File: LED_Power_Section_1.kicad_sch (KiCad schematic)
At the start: 9 parts, among them IC3 A6214KLKTR-T

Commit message: reviewed
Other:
- moved on the sheet: C1, C6, C7, C8, D2, IC3, L2, R4, R5

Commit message: first complete version schematics
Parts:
- added C11, C24, C28, C32, C36: 33 uF, Capacitor_THT:CP_Radial_D8.0mm_P3.50mm, symbol PCM_SL_Devices:Capacitor_PO
- added C21, C25, C29, C33, C37: 4.7 uF, Capacitor_THT:C_Disc_D3.0mm_W2.0mm_P2.50mm, symbol PCM_SL_Devices:Capacitor_NP
- added C22, C26, C30, C34, C38: 1 uF, Capacitor_SMD:C_1206_3216Metric_Pad1.33x1.80mm_HandSolder, symbol PCM_SL_Devices:Capacitor_NP
- added C23, C27, C31, C35, C39: 0.1 uF, Capacitor_SMD:C_1206_3216Metric_Pad1.33x1.80mm_HandSolder, symbol PCM_SL_Devices:Capacitor_NP
- added D3, D4, D5, D6, D7: 30V 2A, ADC:SODFL3516X90N, symbol PCM_4ms_Diode:B140-E3
- added IC4, IC5, IC6, IC7, IC8: A6214KLKTR-T, LED_Driver:SOP100P600X165-11N, symbol A6214KLKTR-T:A6214KLKTR-T
- added L3, L4, L5, L6, L7: 47 uH 2A, ADC:CDRH105RNP151NC, symbol Device:L
- added R11, R13, R15, R17, R19: 442k, Resistor_SMD:R_1206_3216Metric_Pad1.30x1.75mm_HandSolder, symbol PCM_SL_Resistors:Resistor
- added R12, R14, R16, R18, R20: R120 or R260, Resistor_THT:R_Radial_Power_L16.1mm_W9.0mm_P7.37mm, symbol PCM_SL_Resistors:Resistor
- D2: value 60V 2A -> 30V 2A
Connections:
- net +12V: now also C11.1, C21.2, C24.1, C25.2, C28.1, C29.2, C32.1, C33.2, C36.1, C37.2, IC4.1 (VIN), IC5.1 (VIN), IC6.1 (VIN), IC7.1 (VIN), IC8.1 (VIN), R11.2, R13.2, R15.2, R17.2, R19.2
- net GND: now also C11.2, C21.1, C22.1, C24.2, C25.1, C26.1, C28.2, C29.1, C30.1, C32.2, C33.1, C34.1, C36.2, C37.1, C38.1, D3.2 (A), D4.2 (A), D5.2 (A), D6.2 (A), D7.2 (A), IC4.11 (GND_2), IC4.6 (GND_1), IC5.11 (GND_2), IC5.6 (GND_1), IC6.11 (GND_2), IC6.6 (GND_1), IC7.11 (GND_2), IC7.6 (GND_1), IC8.11 (GND_2), IC8.6 (GND_1)
- new net: C31.2, D5.1 (K), IC6.10 (SW), L5.1
- new net: C27.2, D4.1 (K), IC5.10 (SW), L4.1
- new net: C39.2, D7.1 (K), IC8.10 (SW), L7.1
- new net: IC8.2 (TON), R19.1
- new net: C38.2, IC8.4 (ADIM), IC8.5 (VCC)
- new net: C39.1, IC8.9 (BOOT)
- new net: C30.2, IC6.4 (ADIM), IC6.5 (VCC)
- new net: C26.2, IC5.4 (ADIM), IC5.5 (VCC)
- new net: IC6.2 (TON), R15.1
- new net: C31.1, IC6.9 (BOOT)
- new net: IC4.2 (TON), R11.1
- new net: C34.2, IC7.4 (ADIM), IC7.5 (VCC)
- new net: IC5.2 (TON), R13.1
- new net: C27.1, IC5.9 (BOOT)
- new net: C35.2, D6.1 (K), IC7.10 (SW), L6.1
- new net: C23.2, D3.1 (K), IC4.10 (SW), L3.1
- new net: C35.1, IC7.9 (BOOT)
- new net: C22.2, IC4.4 (ADIM), IC4.5 (VCC)
- new net: C23.1, IC4.9 (BOOT)
- new net: IC7.2 (TON), R17.1
- new net I_LED_1: IC4.8 (CSH), L3.2, R12.2
- new net I_LED_2: IC5.8 (CSH), L4.2, R14.2
- new net I_LED_3: IC6.8 (CSH), L5.2, R16.2
- new net I_LED_4: IC7.8 (CSH), L6.2, R18.2
- new net I_LED_5: IC8.8 (CSH), L7.2, R20.2
- new net LED_1: IC4.7 (CSL), R12.1
- new net LED_2: IC5.7 (CSL), R14.1
- new net LED_3: IC6.7 (CSL), R16.1
- new net LED_4: IC7.7 (CSL), R18.1
- new net LED_5: IC8.7 (CSL), R20.1
- new net PWM_1: IC4.3 (EN/PWM)
- new net PWM_2: IC5.3 (EN/PWM)
- new net PWM_3: IC6.3 (EN/PWM)
- new net PWM_4: IC7.3 (EN/PWM)
- new net PWM_5: IC8.3 (EN/PWM)
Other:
- moved on the sheet: C1, C6, C7, C8, D2, IC3, L2, R4, R5

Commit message: Changed footprints of passive elements, reviewed
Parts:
- removed C1, C11, C24, C28, C32, C36: 33 uF, Capacitor_THT:CP_Radial_D8.0mm_P3.50mm, symbol PCM_SL_Devices:Capacitor_PO
- removed C21, C25, C29, C33, C37, C6: 4.7 uF, Capacitor_THT:C_Disc_D3.0mm_W2.0mm_P2.50mm, symbol PCM_SL_Devices:Capacitor_NP
- removed C22, C26, C30, C34, C38, C7: 1 uF, Capacitor_SMD:C_1206_3216Metric_Pad1.33x1.80mm_HandSolder, symbol PCM_SL_Devices:Capacitor_NP
- removed C23, C27, C31, C35, C39, C8: 0.1 uF, Capacitor_SMD:C_1206_3216Metric_Pad1.33x1.80mm_HandSolder, symbol PCM_SL_Devices:Capacitor_NP
- added C14, C15, C16, C29, C30, C31: 22uF, Capacitor_SMD:C_0805_2012Metric_Pad1.18x1.45mm_HandSolder, symbol Device:C_Small
- added C17, C18, C19, C32, C33, C34: 4,7uF, Capacitor_SMD:C_0603_1608Metric_Pad1.08x0.95mm_HandSolder, symbol Device:C_Small
- added C20, C21, C22, C35, C36, C37: 1uF, Capacitor_SMD:C_0603_1608Metric_Pad1.08x0.95mm_HandSolder, symbol Device:C_Small
- added C23, C24, C25, C26, C27, C28, C38, C39, C40, C41, C42, C43: 100nF, Capacitor_SMD:C_0603_1608Metric_Pad1.08x0.95mm_HandSolder, symbol Device:C_Small
- D1: renamed from D4; value 30V 2A -> SS34; footprint ADC:SODFL3516X90N -> Diode_SMD:D_SMA; Specifications SCHOTTKY Diode SMA Vrrm>=40V If>=1.0A, Ifsm>=1.5A -> 40V, 2A
- D2: renamed from D6; value 30V 2A -> SS34; footprint ADC:SODFL3516X90N -> Diode_SMD:D_SMA; Specifications SCHOTTKY Diode SMA Vrrm>=40V If>=1.0A, Ifsm>=1.5A -> 40V, 2A
- D3: renamed from D2; value 30V 2A -> SS34; footprint ADC:SODFL3516X90N -> Diode_SMD:D_SMA; Specifications SCHOTTKY Diode SMA Vrrm>=40V If>=1.0A, Ifsm>=1.5A -> 40V, 2A
- D4: renamed from D7; value 30V 2A -> SS34; footprint ADC:SODFL3516X90N -> Diode_SMD:D_SMA; Specifications SCHOTTKY Diode SMA Vrrm>=40V If>=1.0A, Ifsm>=1.5A -> 40V, 2A
- D5: renamed from D3; value 30V 2A -> SS34; footprint ADC:SODFL3516X90N -> Diode_SMD:D_SMA; Specifications SCHOTTKY Diode SMA Vrrm>=40V If>=1.0A, Ifsm>=1.5A -> 40V, 2A
- D6: renamed from D5; value 30V 2A -> SS34; footprint ADC:SODFL3516X90N -> Diode_SMD:D_SMA; Specifications SCHOTTKY Diode SMA Vrrm>=40V If>=1.0A, Ifsm>=1.5A -> 40V, 2A
- R11: renamed from R19; footprint Resistor_SMD:R_1206_3216Metric_Pad1.30x1.75mm_HandSolder -> Resistor_SMD:R_0603_1608Metric_Pad0.98x0.95mm_HandSolder
- R12: renamed from R11; footprint Resistor_SMD:R_1206_3216Metric_Pad1.30x1.75mm_HandSolder -> Resistor_SMD:R_0603_1608Metric_Pad0.98x0.95mm_HandSolder
- R13: renamed from R15; footprint Resistor_SMD:R_1206_3216Metric_Pad1.30x1.75mm_HandSolder -> Resistor_SMD:R_0603_1608Metric_Pad0.98x0.95mm_HandSolder
- R5: renamed from R13; footprint Resistor_SMD:R_1206_3216Metric_Pad1.30x1.75mm_HandSolder -> Resistor_SMD:R_0603_1608Metric_Pad0.98x0.95mm_HandSolder
- R6: renamed from R17; footprint Resistor_SMD:R_1206_3216Metric_Pad1.30x1.75mm_HandSolder -> Resistor_SMD:R_0603_1608Metric_Pad0.98x0.95mm_HandSolder
- R7: renamed from R4; footprint Resistor_SMD:R_1206_3216Metric_Pad1.30x1.75mm_HandSolder -> Resistor_SMD:R_0603_1608Metric_Pad0.98x0.95mm_HandSolder
- renumbered IC5 to IC2, IC7 to IC3, IC3 to IC4, IC8 to IC5, IC4 to IC6, IC6 to IC7, L4 to L1, L6 to L2, L2 to L3, L7 to L4, L3 to L5, L5 to L6, R5 to R10, R20 to R14, R12 to R15, R14 to R8, R18 to R9
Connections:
- net +12V: now also C14.2, C15.2, C16.2, C17.1, C18.1, C19.1, C29.2, C30.2, C31.2, C32.1, C33.1, C34.1
- net GND: now also C14.1, C15.1, C16.1, C17.2, C18.2, C19.2, C20.2, C21.2, C22.2, C26.2, C27.2, C28.2, C29.1, C30.1, C31.1, C32.2, C33.2, C34.2, C35.2, C36.2, C37.2, C41.2, C42.2, C43.2
- net LED_0: now also C28.1
- net LED_1: now also C42.1
- net LED_2: now also C26.1
- net LED_3: now also C43.1
- net LED_4: now also C27.1
- net LED_5: now also C41.1
- net at D6.1 (K), IC7.10 (SW), L6.1: now also C40.1
- net at D1.1 (K), IC2.10 (SW), L1.1: now also C23.1
- net at D4.1 (K), IC5.10 (SW), L4.1: now also C38.1
- net at IC5.4 (ADIM), IC5.5 (VCC): now also C35.1
- net at IC5.9 (BOOT): now also C38.2
- net at IC7.4 (ADIM), IC7.5 (VCC): now also C37.1
- net at IC2.4 (ADIM), IC2.5 (VCC): now also C20.1
- net at IC7.9 (BOOT): now also C40.2
- net at IC3.4 (ADIM), IC3.5 (VCC): now also C21.1
- net at IC2.9 (BOOT): now also C23.2
- net at D2.1 (K), IC3.10 (SW), L2.1: now also C24.1
- net at D5.1 (K), IC6.10 (SW), L5.1: now also C39.1
- net at IC3.9 (BOOT): now also C24.2
- net at IC4.9 (BOOT): now also C25.2
- net at D3.1 (K), IC4.10 (SW), L3.1: now also C25.1
- net at IC6.4 (ADIM), IC6.5 (VCC): now also C36.1
- net at IC6.9 (BOOT): now also C39.2
- net at IC4.4 (ADIM), IC4.5 (VCC): now also C22.1

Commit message: wip
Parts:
- removed C14, C15, C16, C29, C30, C31: 22uF, Capacitor_SMD:C_0805_2012Metric_Pad1.18x1.45mm_HandSolder, symbol Device:C_Small
- removed C17, C18, C19, C32, C33, C34: 4,7uF, Capacitor_SMD:C_0603_1608Metric_Pad1.08x0.95mm_HandSolder, symbol Device:C_Small
- removed C20, C21, C22, C35, C36, C37: 1uF, Capacitor_SMD:C_0603_1608Metric_Pad1.08x0.95mm_HandSolder, symbol Device:C_Small
- removed C23, C24, C25, C26, C27, C28, C38, C39, C40, C41, C42, C43: 100nF, Capacitor_SMD:C_0603_1608Metric_Pad1.08x0.95mm_HandSolder, symbol Device:C_Small
- removed D1, D2, D3, D4, D5, D6: SS34, Diode_SMD:D_SMA, symbol PCM_4ms_Diode:B140-E3
- removed IC2, IC3, IC4, IC5, IC6, IC7: A6214KLKTR-T, LED_Driver:SOP100P600X165-11N, symbol A6214KLKTR-T:A6214KLKTR-T
- removed L1, L2, L3, L4, L5, L6: 47 uH 2A, ADC:CDRH105RNP151NC, symbol Device:L
- removed R10, R14, R15, R16, R8, R9: R120 or R260, Resistor_THT:R_Radial_Power_L16.1mm_W9.0mm_P7.37mm, symbol PCM_SL_Resistors:Resistor
- removed R11, R12, R13, R5, R6, R7: 442k, Resistor_SMD:R_0603_1608Metric_Pad0.98x0.95mm_HandSolder, symbol PCM_SL_Resistors:Resistor
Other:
- added sheet LED_DRIVER_1 (Led_driver.kicad_sch)
- added sheet LED_DRIVER_2 (Led_driver.kicad_sch)
- added sheet LED_DRIVER_3 (Led_driver.kicad_sch)
- added sheet LED_DRIVER_4 (Led_driver.kicad_sch)
- added sheet LED_DRIVER_5 (Led_driver.kicad_sch)
- added sheet LED_DRIVER_6 (Led_driver.kicad_sch)
- note removed: "If RGB diodes used please solder R260 resistor as current limiter."

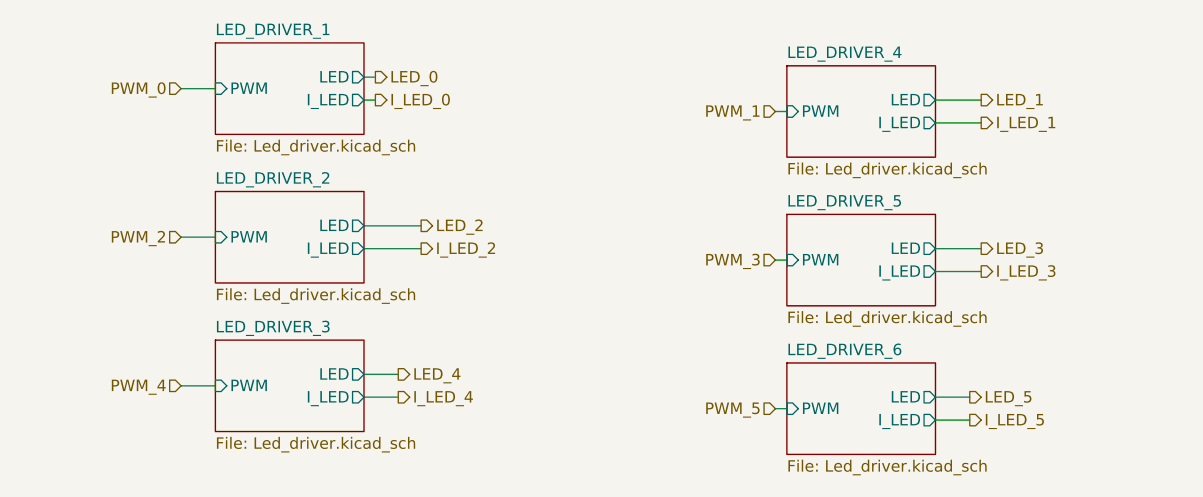
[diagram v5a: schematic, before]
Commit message: Added current sense amplifier, reduced one ADC, changed elec cap to tantals, to review
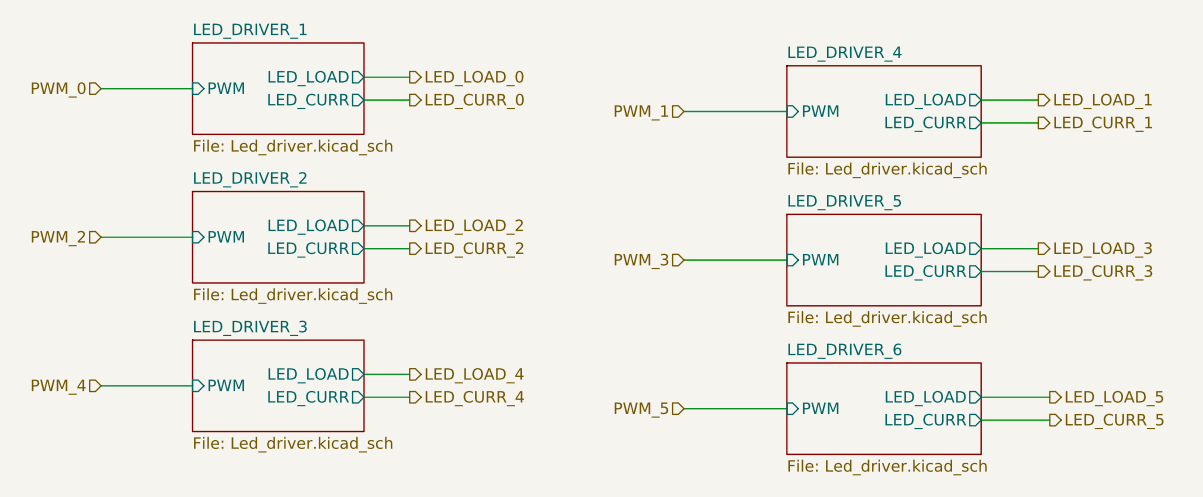
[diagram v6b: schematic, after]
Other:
- sheet LED_DRIVER_1 ports: added LED_CURR, LED_LOAD; removed I_LED, LED
- sheet LED_DRIVER_2 ports: added LED_CURR, LED_LOAD; removed I_LED, LED
- sheet LED_DRIVER_3 ports: added LED_CURR, LED_LOAD; removed I_LED, LED
- sheet LED_DRIVER_4 ports: added LED_CURR, LED_LOAD; removed I_LED, LED
- sheet LED_DRIVER_5 ports: added LED_CURR, LED_LOAD; removed I_LED, LED
- sheet LED_DRIVER_6 ports: added LED_CURR, LED_LOAD; removed I_LED, LED
